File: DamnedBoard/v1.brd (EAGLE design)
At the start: 50.8 x 16.5 mm, 22 parts, among them J1 CORTEX_DEBUG_SMD, J2 I_TEST, J3 TEST, U1 EFM32ZG108, U2 MAX44009EDT+T21-0490D-M

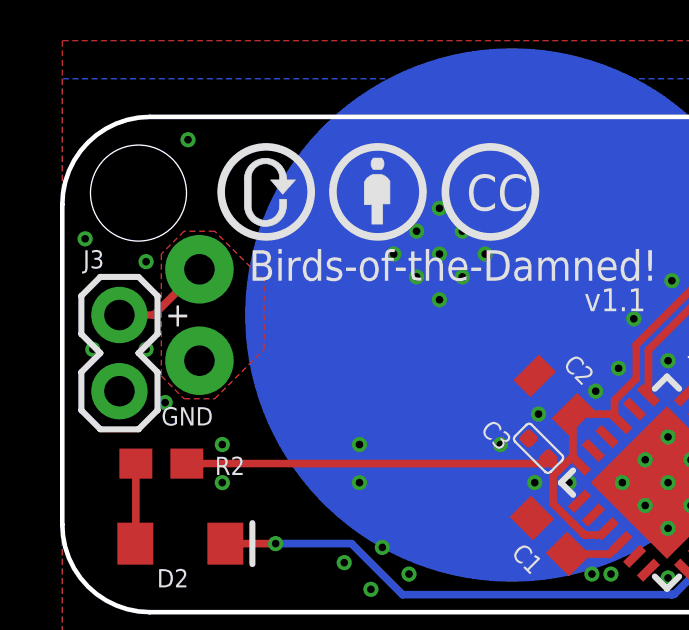
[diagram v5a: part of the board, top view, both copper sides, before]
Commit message: Working EM4 version of the firmware.
Also increased pullups to 1.8K for lower power.
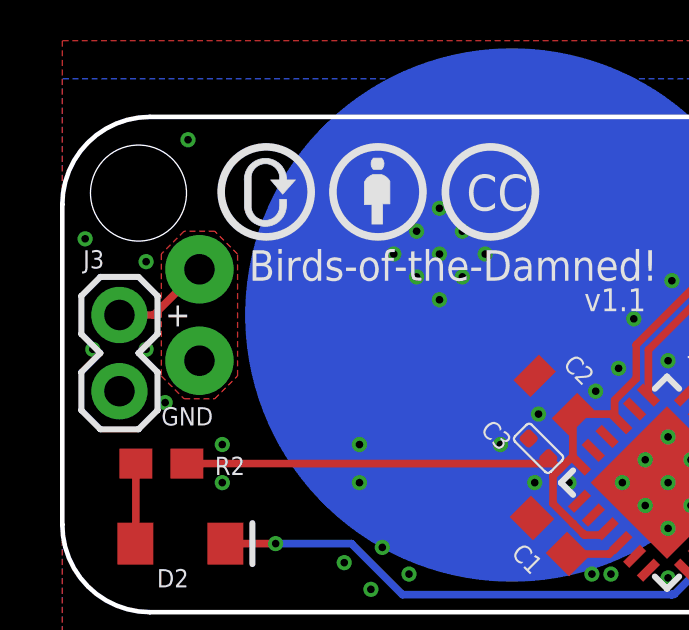
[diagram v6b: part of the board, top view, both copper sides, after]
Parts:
- R3, R4: value 1K -> 1.8K
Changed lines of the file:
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@@
 </element>
 <element name="U$2" library="boneyard" package="32BITS_LOGO" value="" x="45.847" y="3.556" rot="MR0"/>
-<element name="R3" library="Seeed-Resistor" library_urn="urn:adsk.eagle:library:474" package="R0402" package3d_urn="urn:adsk.eagle:package:32792/1" value="1K" x="25.4" y="1.3155" smashed="yes">
+<element name="R3" library="Seeed-Resistor" library_urn="urn:adsk.eagle:library:474" package="R0402" package3d_urn="urn:adsk.eagle:package:32792/1" value="1.8K" x="25.4" y="1.3155" smashed="yes">
 <attribute name="MPN" value="RC0402JR-071KL" x="25.4" y="1.3155" size="1.778" layer="27" display="off"/>
 <attribute name="NAME" x="26.4975" y="0.381" size="0.6096" layer="25" ratio="20"/>
 </element>
-<element name="R4" library="Seeed-Resistor" library_urn="urn:adsk.eagle:library:474" package="R0402" package3d_urn="urn:adsk.eagle:package:32792/1" value="1K" x="26.543" y="2.0225" smashed="yes" rot="R180">
+<element name="R4" library="Seeed-Resistor" library_urn="urn:adsk.eagle:library:474" package="R0402" package3d_urn="urn:adsk.eagle:package:32792/1" value="1.8K" x="26.543" y="2.0225" smashed="yes" rot="R180">
 <attribute name="MPN" value="RC0402JR-071KL" x="26.543" y="2.0225" size="1.778" layer="27" rot="R180" display="off"/>
 <attribute name="NAME" x="24.9015" y="1.143" size="0.6096" layer="25" ratio="20" rot="R180"/>
@@
 <vertex x="4.064" y="7.112"/>
 <vertex x="5.08" y="7.112"/>
-<vertex x="6.731" y="8.763"/>
-<vertex x="6.731" y="11.049"/>
+<vertex x="5.842" y="7.874"/>
+<vertex x="5.842" y="11.938"/>
 <vertex x="5.08" y="12.7"/>
 <vertex x="4.064" y="12.7"/>

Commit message: Moving to ADC for trimmer.
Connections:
- net ADJ: now also U1.13; no longer U1.4
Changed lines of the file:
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@@
 <?xml version="1.0" encoding="utf-8"?>
 <!DOCTYPE eagle SYSTEM "eagle.dtd">
-<eagle version="8.3.1">
+<eagle version="8.3.2">
 <drawing>
 <settings>
@@
 </signal>
 <signal name="ADJ">
-<contactref element="U1" pad="4"/>
 <contactref element="R5" pad="2"/>
 <wire x1="26.125965625" y1="6.62939375" x2="26.334271875" y2="6.8377" width="0.2032" layer="1"/>
@@
 <wire x1="22.86" y1="6.62939375" x2="22.0472" y2="6.62939375" width="0.2032" layer="1"/>
 <wire x1="22.0472" y1="6.62939375" x2="21.73338125" y2="6.315575" width="0.2032" layer="1"/>
-<wire x1="21.73338125" y1="6.315575" x2="21.694853125" y2="6.315575" width="0.2032" layer="1"/>
+<contactref element="U1" pad="13"/>
+<wire x1="17.24008125" y1="3.69928125" x2="21.73338125" y2="6.315575" width="0" layer="19" extent="1-1"/>
 </signal>
 <signal name="ADJ_PWR">

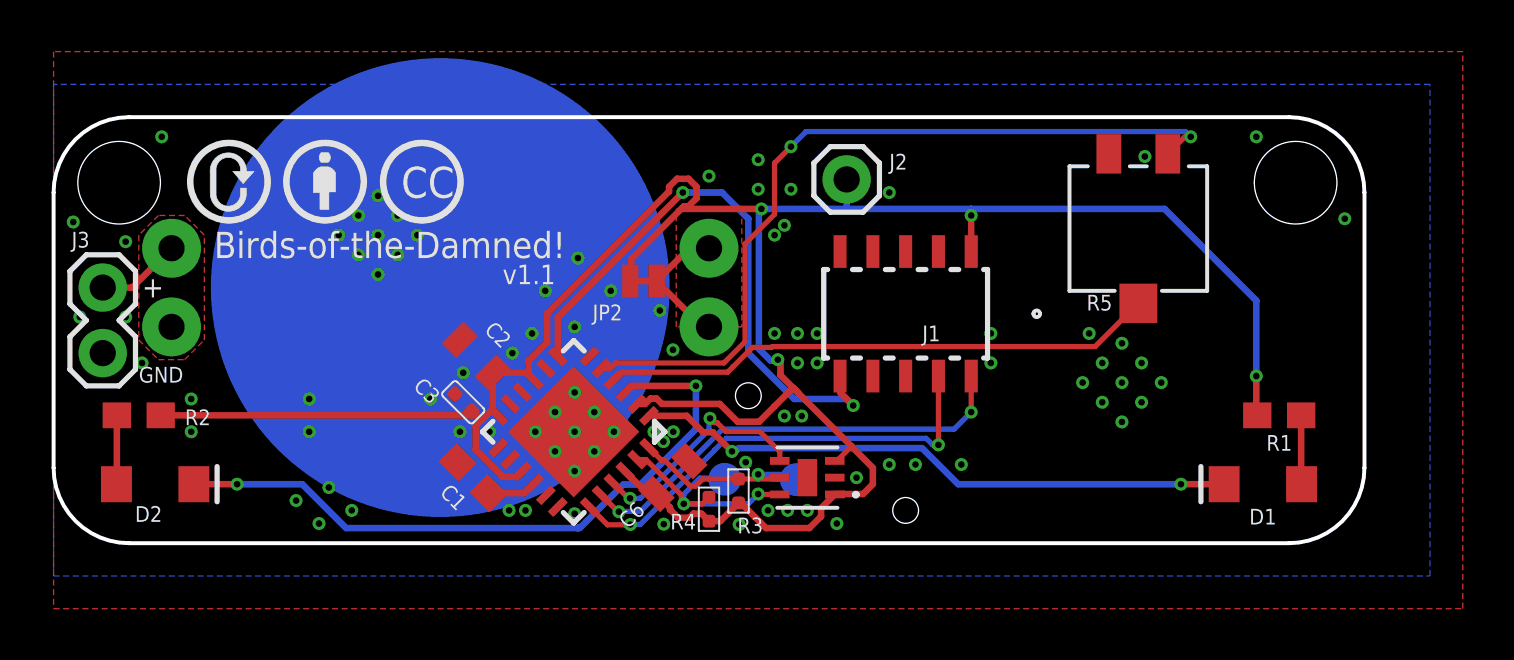
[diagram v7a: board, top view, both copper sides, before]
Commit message: V1.1 locked. Ordered from OSH park.
All perphierals working in the firmware. Just need to finish some features and tune.
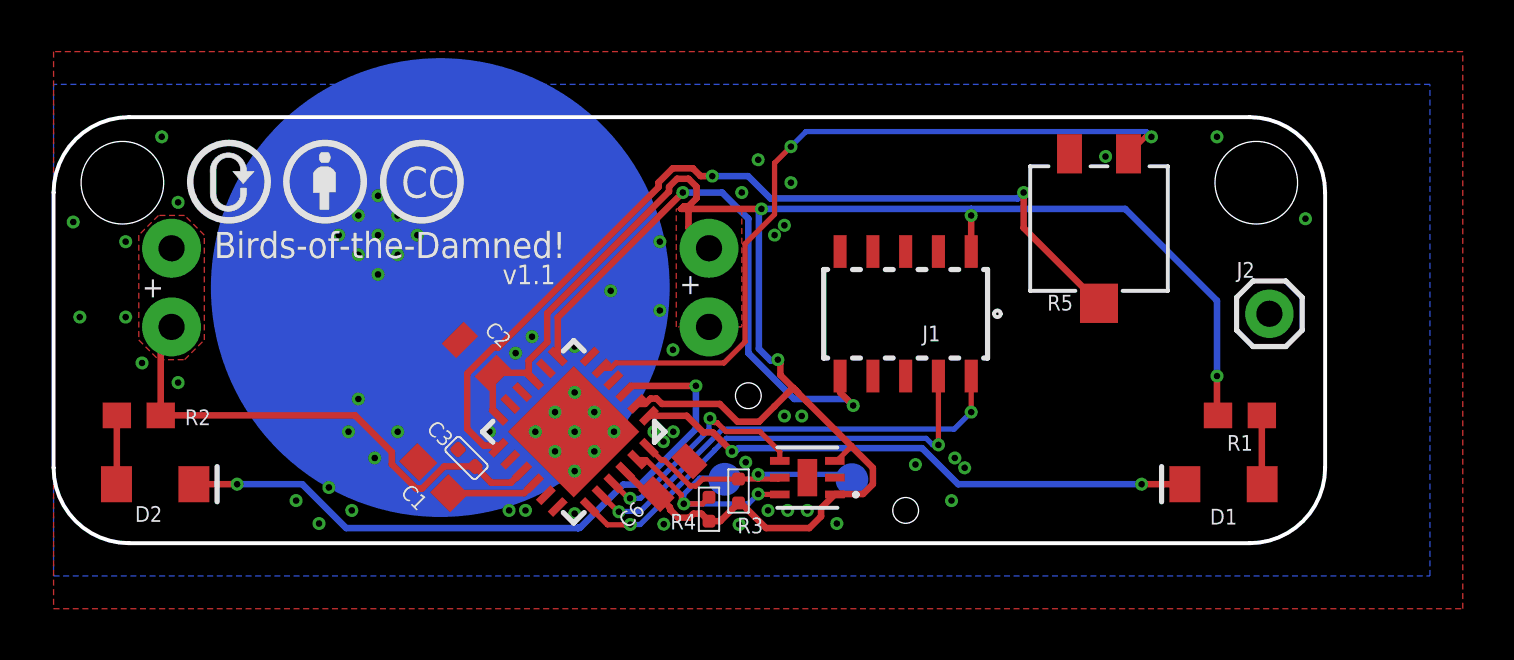
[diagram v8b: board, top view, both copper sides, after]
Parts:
- removed J3: TEST, SparkFun-Connectors:1X02
- removed JP2: JUMPER-SMT_2_NC_TRACE_NO-SILK, SparkFun-Jumpers:SMT-JUMPER_2_NC_TRACE_NO-SILK
- J2: value I_TEST -> GND
- moved J2 17.2 mm to (47.1, 8.89)
- moved U$2 3.81 mm to (43.6, 6.60)
- moved C3 2.16 mm to (16.0, 3.30)
- moved TP2 2.16 mm to (30.9, 2.46)
- moved C1 1.52 mm to (14.7, 2.54)
- moved D1 1.52 mm to (45.3, 2.29)
- moved R1 1.52 mm to (46.0, 4.95)
- moved R5 1.52 mm to (40.5, 12.2)
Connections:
- removed net +L: G1.P$1, G1.P$2, JP2.2
- removed net +R: G1.P$3, G1.P$4, J3.2
- net VCC: now also G1.P$1, G1.P$2, G1.P$3, G1.P$4; no longer J2.1, JP2.1
- net VSS: now also J2.1; no longer J3.1
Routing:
- net ADJ: track 21.7 -> 34.7 mm, vias 0 -> 2
- net +L: track 5.33 -> 0.00 mm
- net +R: track 3.30 -> 0.00 mm
- net SCL: track 7.53 -> 9.89 mm
- net EYE_L: track 23.5 -> 22.0 mm
- net ADJ_PWR: track 31.3 -> 29.7 mm
- net DCP: track 1.92 -> 3.44 mm
- net VSS: vias 90 -> 69
- added copper zone on layer 1, net VCC
- removed copper zone on layer 1, net +L
- removed copper zone on layer 1, net +R
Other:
- board size 50.8 x 16.5 mm -> 49.3 x 16.5 mm
